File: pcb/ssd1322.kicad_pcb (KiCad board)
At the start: 2 copper layers, 40 x 25 mm, 34 parts, among them J1 Display Connector Input, J2 SSD1322 30-Pin Connector, J3 USB_C_Receptacle_USB2.0_16P, U1 AP2112K-3.3, U2 ESP32-S3-WROOM-1, U3 MT3608

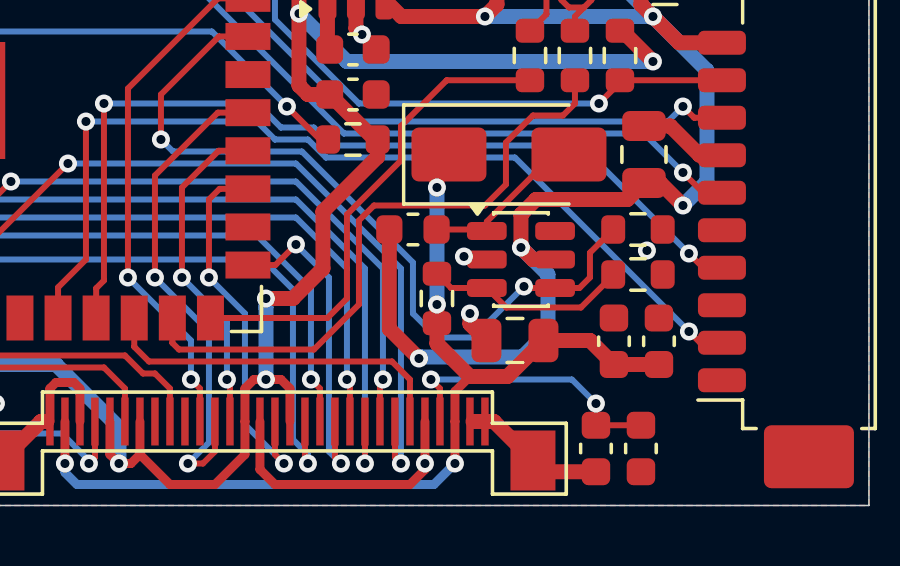
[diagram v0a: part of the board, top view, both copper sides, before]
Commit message: SSD1327 PCB routing
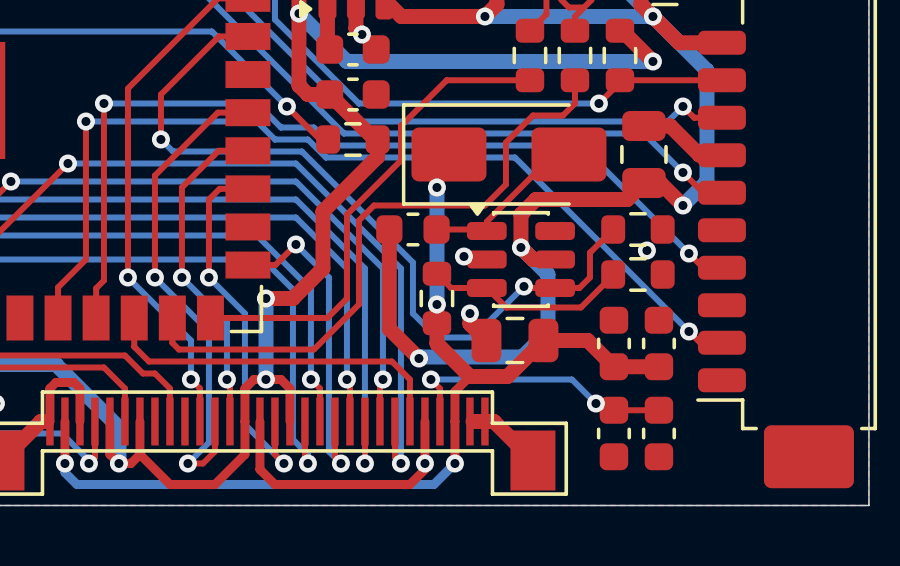
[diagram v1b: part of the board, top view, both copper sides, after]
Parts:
- moved C2 0.78 mm to (63.0, 52.6)
- moved C3 0.78 mm to (61.5, 52.6)
- moved C12 0.08 mm to (63.0, 49.6)
- moved C13 0.08 mm to (61.5, 49.6)
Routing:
- net GND: track 34.6 -> 32.3 mm
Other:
- board text added: "Jonathan Ho 2026-03-12"
- board text added: "SSD1322 Display Adapter"
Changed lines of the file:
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@@
 	(footprint "Capacitor_SMD:C_0603_1608Metric"
 		(layer "F.Cu")
-		(at 61.5 49.525 90)
+		(at 61.5 49.6 90)
 		(descr "Capacitor SMD 0603 (1608 Metric), square (rectangular) end terminal, IPC-7351 nominal, (Body size source: IPC-SM-782 page 76, https://www.pcb-3d.com/wordpress/wp-content/uploads/ipc-sm-782a_amendment_1_and_2.pdf), generated with kicad-footprint-generator")
 		(tags "capacitor")
 		(property "Reference" "C13"
-			(at 49.525 -61.5 0)
+			(at 49.6 -61.5 0)
 			(layer "F.SilkS")
 			(effects
@@
 		)
 		(property "Value" "0.1uF (25V)"
-			(at 49.525 -61.5 0)
+			(at 49.6 -61.5 0)
 			(layer "F.Fab")
 			(effects
@@
 		)
 		(fp_text user "${REFERENCE}"
-			(at 49.525 -61.5 0)
+			(at 49.6 -61.5 0)
 			(layer "F.Fab")
 			(effects
@@
 	(footprint "Capacitor_SMD:C_0603_1608Metric"
 		(layer "F.Cu")
-		(at 60.9 53.1 -90)
+		(at 61.5 52.6 -90)
 		(descr "Capacitor SMD 0603 (1608 Metric), square (rectangular) end terminal, IPC-7351 nominal, (Body size source: IPC-SM-782 page 76, https://www.pcb-3d.com/wordpress/wp-content/uploads/ipc-sm-782a_amendment_1_and_2.pdf), generated with kicad-footprint-generator")
 		(tags "capacitor")
 		(property "Reference" "C3"
-			(at -53.1 60.9 0)
+			(at -52.6 61.5 0)
 			(layer "F.SilkS")
 			(effects
@@
 		)
 		(property "Value" "0.1uF (25V)"
-			(at -53.1 60.9 0)
+			(at -52.6 61.5 0)
 			(layer "F.Fab")
 			(effects
@@
 		)
 		(fp_text user "${REFERENCE}"
-			(at -53.1 60.9 0)
+			(at -52.6 61.5 0)
 			(layer "F.Fab")
 			(effects
@@
 	(footprint "Capacitor_SMD:C_0603_1608Metric"
 		(layer "F.Cu")
-		(at 63 49.525 90)
+		(at 63 49.6 90)
 		(descr "Capacitor SMD 0603 (1608 Metric), square (rectangular) end terminal, IPC-7351 nominal, (Body size source: IPC-SM-782 page 76, https://www.pcb-3d.com/wordpress/wp-content/uploads/ipc-sm-782a_amendment_1_and_2.pdf), generated with kicad-footprint-generator")
 		(tags "capacitor")
 		(property "Reference" "C12"
-			(at 49.525 -63 0)
+			(at 49.6 -63 0)
 			(layer "F.SilkS")
 			(effects
@@
 		)
 		(property "Value" "10uF (25V)"
-			(at 49.525 -63 0)
+			(at 49.6 -63 0)
 			(layer "F.Fab")
 			(effects
@@
 		)
 		(fp_text user "${REFERENCE}"
-			(at 49.525 -63 0)
+			(at 49.6 -63 0)
 			(layer "F.Fab")
 			(effects
@@
 	(footprint "Capacitor_SMD:C_0603_1608Metric"
 		(layer "F.Cu")
-		(at 62.4 53.1 -90)
+		(at 63 52.6 -90)
 		(descr "Capacitor SMD 0603 (1608 Metric), square (rectangular) end terminal, IPC-7351 nominal, (Body size source: IPC-SM-782 page 76, https://www.pcb-3d.com/wordpress/wp-content/uploads/ipc-sm-782a_amendment_1_and_2.pdf), generated with kicad-footprint-generator")
 		(tags "capacitor")
 		(property "Reference" "C2"
-			(at -53.1 62.4 0)
+			(at -52.6 63 0)
 			(layer "F.SilkS")
 			(effects
@@
 		)
 		(property "Value" "4.7uF (25V)"
-			(at -53.1 62.4 0)
+			(at -52.6 63 0)
 			(layer "F.Fab")
 			(effects
@@
 		)
 		(fp_text user "${REFERENCE}"
-			(at -53.1 62.4 0)
+			(at -52.6 63 0)
 			(layer "F.Fab")
 			(effects
@@
 		(layer "Edge.Cuts")
 	)
+	(gr_text "SSD1322 Display Adapter"
+		(at 68 32 0)
+		(layer "B.SilkS")
+		(effects
+			(font
+				(size 1 1)
+				(thickness 0.2)
+				(bold yes)
+			)
+			(justify left top mirror)
+		)
+	)
+	(gr_text "Jonathan Ho\n2026-03-12"
+		(at 68 34 0)
+		(layer "B.SilkS")
+		(effects
+			(font
+				(size 1 1)
+				(thickness 0.125)
+			)
+			(justify left top mirror)
+		)
+	)
 	(segment
 		(start 42.9 50.9)
@@
 	)
 	(segment
-		(start 59.175 53.875)
-		(end 58.8 53.5)
-		(width 0.5)
-		(layer "F.Cu")
-		(net 1)
-	)
-	(segment
 		(start 40.975 53.375)
 		(end 41.1 53.5)
@@
 	)
 	(segment
-		(start 60.9 53.875)
-		(end 59.175 53.875)
-		(width 0.5)
-		(layer "F.Cu")
-		(net 1)
-	)
-	(segment
 		(start 42.7 52.2)
 		(end 42.7 51.1)
@@
 	)
 	(segment
-		(start 60.9 52.325)
-		(end 60.9 51.6)
+		(start 61.5 51.825)
+		(end 63 51.825)
+		(width 0.2)
+		(layer "F.Cu")
+		(net 3)
+	)
+	(segment
+		(start 61.5 51.825)
+		(end 61.125 51.825)
 		(width 0.2)
 		(layer "F.Cu")
@@
 	)
 	(segment
-		(start 62.4 52.325)
-		(end 60.9 52.325)
+		(start 61.125 51.825)
+		(end 60.9 51.6)
 		(width 0.2)
 		(layer "F.Cu")
@@
 	)
 	(segment
-		(start 49.9 48.4)
-		(end 49.9 50.8)
-		(width 0.5)
-		(layer "B.Cu")
-		(net 5)
-	)
-	(segment
-		(start 49.9 48.4)
+		(start 49.9 50.8)
 		(end 49.9 48.1)
 		(width 0.5)
@@
 	)
 	(segment
-		(start 59.15 49.5)
-		(end 60.7 49.5)
-		(width 0.5)
-		(layer "F.Cu")
-		(net 6)
-	)
-	(segment
 		(start 56.2 53.6)
 		(end 56.2 52.2)
@@
 	)
 	(segment
+		(start 60.625 49.5)
+		(end 61.5 50.375)
+		(width 0.5)
+		(layer "F.Cu")
+		(net 6)
+	)
+	(segment
 		(start 56.2 52.2)
 		(end 56.2 51.2)
@@
 	)
 	(segment
+		(start 61.5 50.375)
+		(end 63 50.375)
+		(width 0.5)
+		(layer "F.Cu")
+		(net 6)
+	)
+	(segment
 		(start 55.6 43.7)
 		(end 56 43.3)
@@
 	)
 	(segment
-		(start 63 50.3)
-		(end 61.5 50.3)
+		(start 59.15 49.5)
+		(end 60.625 49.5)
 		(width 0.5)
 		(layer "F.Cu")
@@
 		(net 6)
 	)
-	(segment
-		(start 60.7 49.5)
-		(end 61.5 50.3)
-		(width 0.5)
-		(layer "F.Cu")
-		(net 6)
-	)
 	(via
 		(at 56.2 53.6)
@@
 	)
 	(segment
-		(start 55.6 45.9)
-		(end 55.6 44.4)
-		(width 0.5)
-		(layer "B.Cu")
-		(net 6)
-	)
-	(segment
 		(start 55.6 48.3)
-		(end 55.6 45.9)
+		(end 55.6 44.4)
 		(width 0.5)
 		(layer "B.Cu")
@@
 	)
 	(segment
-		(start 48.6 50.8)
-		(end 48.6 49.9)
-		(width 0.2)
-		(layer "B.Cu")
-		(net 18)
-	)
-	(segment
 		(start 48.6 48.9)
 		(end 47.1 47.4)
@@
 	)
 	(segment
-		(start 48.6 49.9)
+		(start 48.6 50.8)
 		(end 48.6 48.9)
 		(width 0.2)

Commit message: Master board PCB routing
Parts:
- C11: value 22uF (25V) -> 22uF
- C12: value 10uF (25V) -> 10uF
- C13, C3: value 0.1uF (25V) -> 0.1uF
- C2: value 4.7uF (25V) -> 4.7uF
- L1: value 22uH (or 10uH) -> 10uH
- R10: value 190k (or 200k) -> 200k
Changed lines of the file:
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@@
 			)
 		)
-		(property "Value" "22uH (or 10uH)"
+		(property "Value" "10uH"
 			(at -54.8 -45.8 0)
 			(layer "F.Fab")
@@
 			)
 		)
-		(property "Value" "0.1uF (25V)"
+		(property "Value" "0.1uF"
 			(at 49.6 -61.5 0)
 			(layer "F.Fab")
@@
 			)
 		)
-		(property "Value" "22uF (25V)"
+		(property "Value" "22uF"
 			(at 58.2 49.5 0)
 			(layer "F.Fab")
@@
 		(sheetname "/ESP32 for SSD1322/")
 		(sheetfile "esp32.kicad_sch")
-		(attr smd)
+		(attr smd exclude_from_bom)
 		(fp_line
 			(start 9.2 -12.9)
@@
 			)
 		)
-		(property "Value" "0.1uF (25V)"
+		(property "Value" "0.1uF"
 			(at -52.6 61.5 0)
 			(layer "F.Fab")
@@
 			)
 		)
-		(property "Value" "10uF (25V)"
+		(property "Value" "10uF"
 			(at 49.6 -63 0)
 			(layer "F.Fab")
@@
 			)
 		)
-		(property "Value" "190k (or 200k)"
+		(property "Value" "200k"
 			(at 48.1 -55.6 0)
 			(layer "F.Fab")
@@
 			)
 		)
-		(property "Value" "4.7uF (25V)"
+		(property "Value" "4.7uF"
 			(at -52.6 63 0)
 			(layer "F.Fab")
@@
 	)
 	(gr_text "SSD1322 Display Adapter"
-		(at 68 32 0)
+		(at 32 32 0)
 		(layer "B.SilkS")
 		(effects
@@
 				(bold yes)
 			)
-			(justify left top mirror)
+			(justify right top mirror)
 		)
 	)
 	(gr_text "Jonathan Ho\n2026-03-12"
-		(at 68 34 0)
+		(at 32 34 0)
 		(layer "B.SilkS")
 		(effects
@@
 				(thickness 0.125)
 			)
-			(justify left top mirror)
+			(justify right top mirror)
 		)
 	)
